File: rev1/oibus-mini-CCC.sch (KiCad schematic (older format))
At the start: 81 parts, among them J1 Conn_01x04_Female, J2 USB_B_Micro, J3 uavcan_5pins, J4 Conn_01x02_Female, P1 TC2030-MCP, Q1 DMG3415U-7, Q2 DMG3415U-7, Q3 DMG3415U-7, SW1 SW_Push, U1 AP2112K-3.3, U10 TPD3E001DRLR, U2 SAM-M8Q, U3 NINA-B311-00B, U4 MCP73831-2-OT, U5 MCP1624T, U6 SHT31-DIS-B, U7 TCAN330, U8 STM32F303CCTx, U9 DW01C-G, Y1 16M, Y2 32kHz

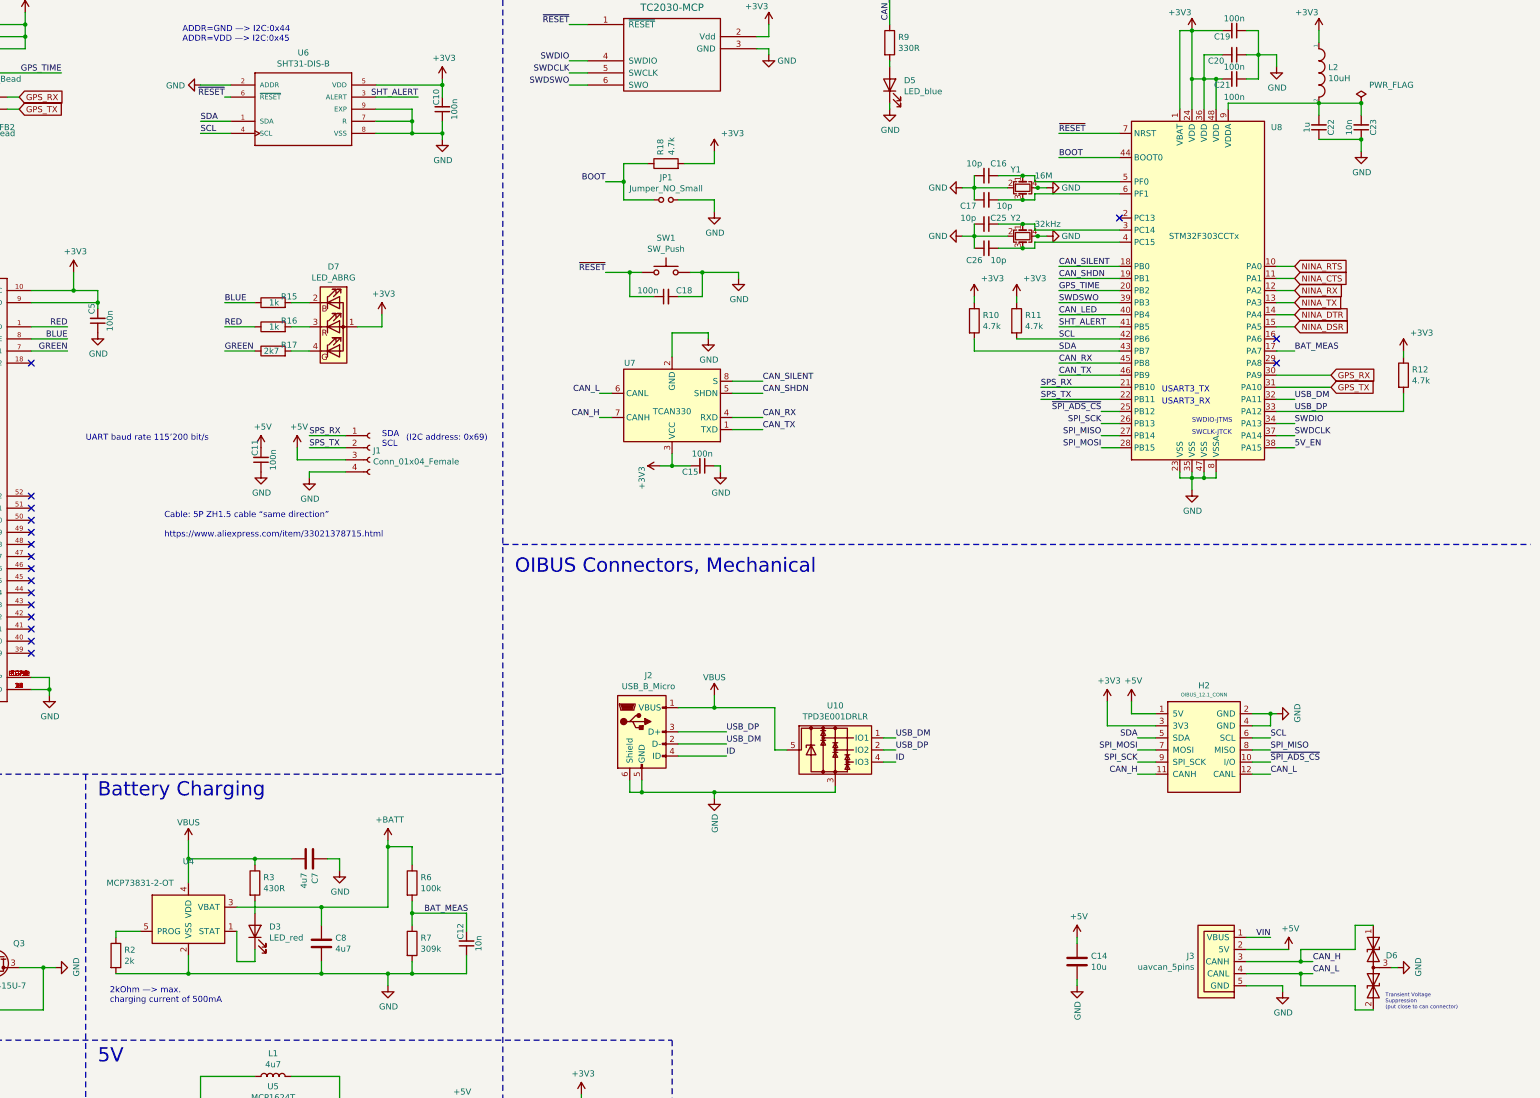
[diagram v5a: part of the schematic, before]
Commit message: finished routing, DRC clear
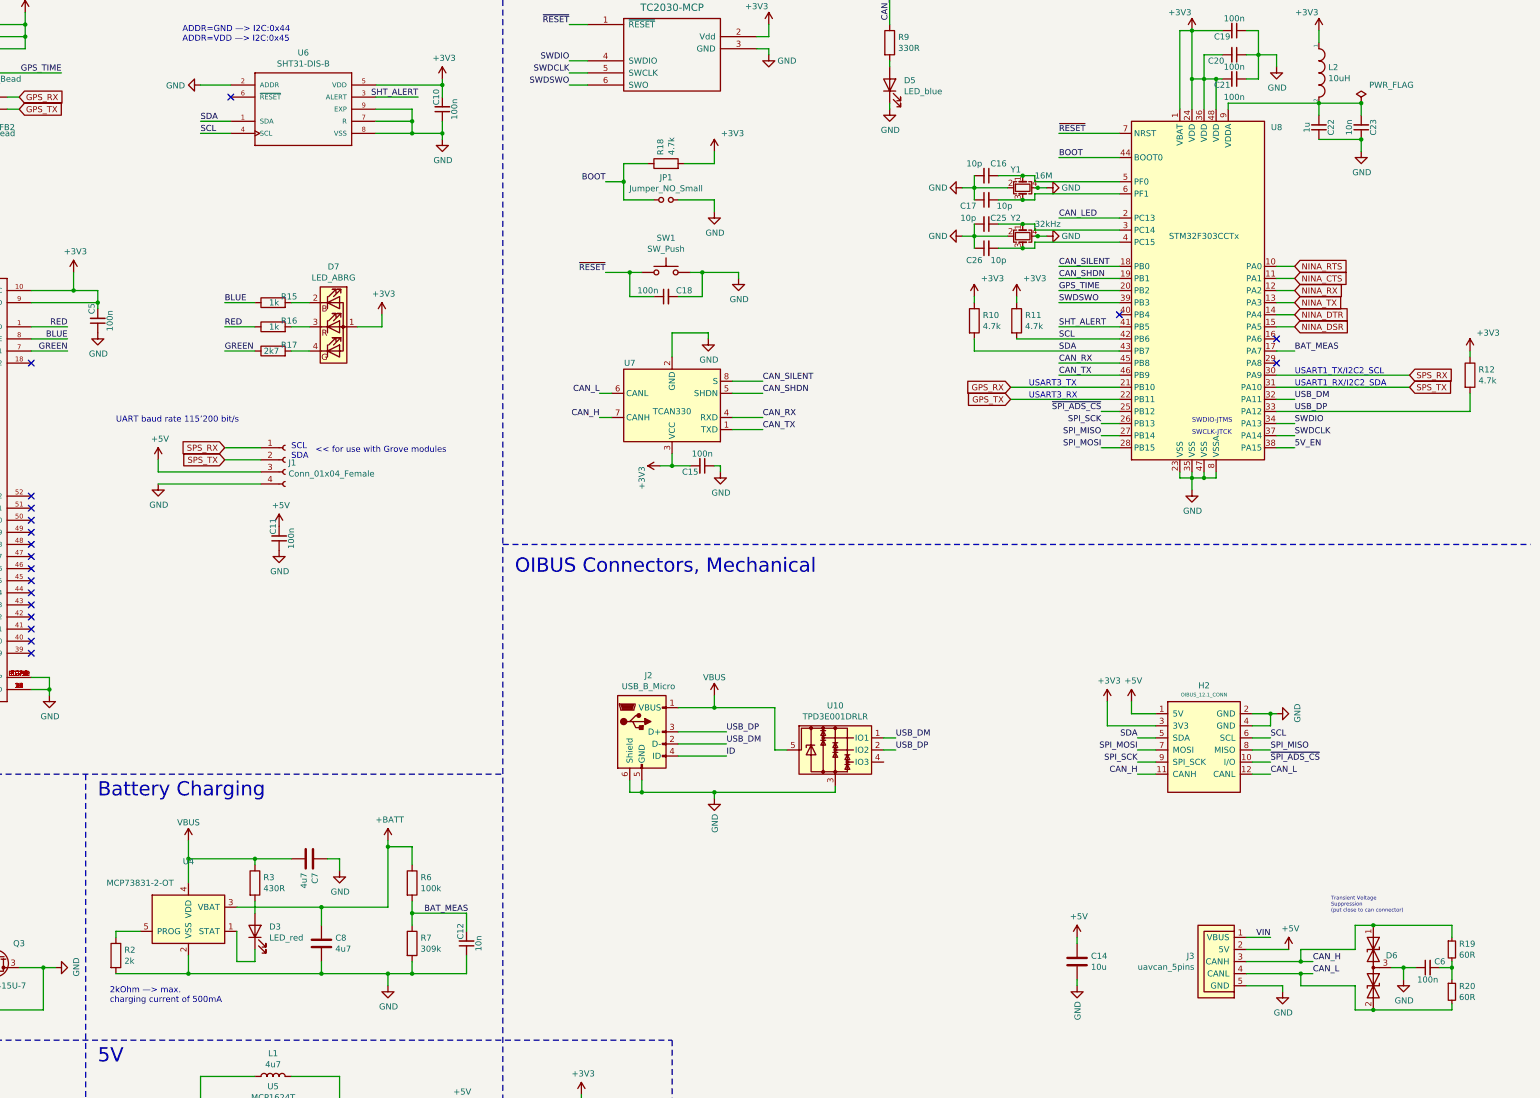
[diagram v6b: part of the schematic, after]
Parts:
- added C6: 100n, Capacitor_SMD:C_0603_1608Metric, symbol Device:C_Small
- added R19, R20: 60R, Resistor_SMD:R_0603_1608Metric, symbol Device:R_Small
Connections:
- net CAN_H: now also R19.1
- net CAN_L: now also R20.2
- net CAN_LED: now also U8.2 (PC13); no longer U8.40 (PB4)
- net GND: now also C6.1
- net GPS_RX: now also U8.21 (PB10); no longer U8.30 (PA9)
- net GPS_TX: now also U8.22 (PB11); no longer U8.31 (PA10)
- net ID: no longer U10.4 (IO3)
- net SPS_RX: now also U8.30 (PA9); no longer U8.21 (PB10)
- net SPS_TX: now also U8.31 (PA10); no longer U8.22 (PB11)
- net ~RESET: no longer U6.6 (~RESET~)
- new net: C6.2, R19.2, R20.1
- no-connect marks 38 -> 39
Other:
- note added: "<< for use with Grove modules"
- note added: "SCL\nSDA"
- note added: "USART1_RX/I2C2_SDA"
- note added: "USART1_TX/I2C2_SCL"
- note removed: "(I2C address: 0x69)"
- note removed: "Cable: 5P ZH1.5 cable “same direction”\n\nhttps://www.aliexpress.com/item/33021378715.html\n"
- note removed: "SDA\nSCL\n"
- moved on the sheet: C11, J1, R12

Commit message: performed some last fixes. Ready to review
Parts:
- removed JP1: Jumper_NO_Small, Jumper:SolderJumper-2_P1.3mm_Open_RoundedPad1.0x1.5mm, symbol Device:Jumper_NO_Small
- BT1: LCSC (none) -> C160352; MPN (none) -> B2B-PH-SM4-TB(LF)(SN)
- C16, C17, C25, C26: MPN 885012006051 -> (none)
- D1: footprint Diode_SMD:D_0603_1608Metric -> Diode_SMD:D_SOD-123F; MPN MBR120 -> MBR120ESFT1G
- FB1, FB2: MPN BLM15HD102SN1 -> BLM15HD102SN1D
- J1: Field4 (none) -> NOTE: MPN is for 10 pieces!; LCSC (none) -> 1125R-4p; MPN (none) -> 110990037
- J2: MPN (none) -> 1050170001
- J3: MPN (none) -> 0530480510
- Q2, Q3: value DMG3415U-7 -> NMOS; MPN DMG3415U-7 -> ZXMN3F30FHTA
- R1, R10, R11, R12, R18, R2, R4, R5, R6, R7: MPN RC0603FR-074K7L -> (none)
- R13, R14, R15, R16, R17, R3, R8, R9: MPN RC0603FR-07330RL -> (none)
- U1: MPN AP2112K-3.3 -> AP2112K-3.3TRG1
- U10: MPN (none) -> TPD3E001DRLR
- U2: MPN SAM-M8Q -> SAM-M8Q-0-10
- U4: MPN MCP73831-2-OT -> MCP73831T-2ATI/OT
- U5: MPN MCP1624T -> MCP1624T-I/CHY
- Y1: MPN FA-238 16.0000MA30X-AG0 -> XXBBBCNANF-16M
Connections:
- net BOOT: now also SW1.1
- net GND: now also Q3.2 (S); no longer Q3.3 (D)
- net ~RESET: no longer SW1.1
- net at Q2.3 (D): now also Q3.3 (D); no longer Q3.2 (S)
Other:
- moved on the sheet: C18, SW1

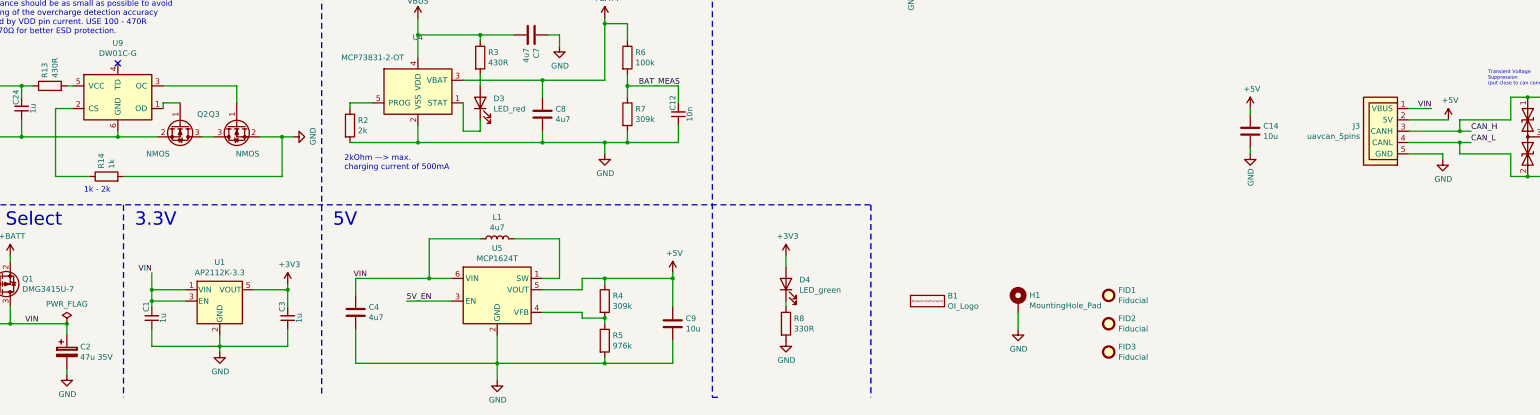
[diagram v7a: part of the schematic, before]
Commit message: moved the grove connector inside
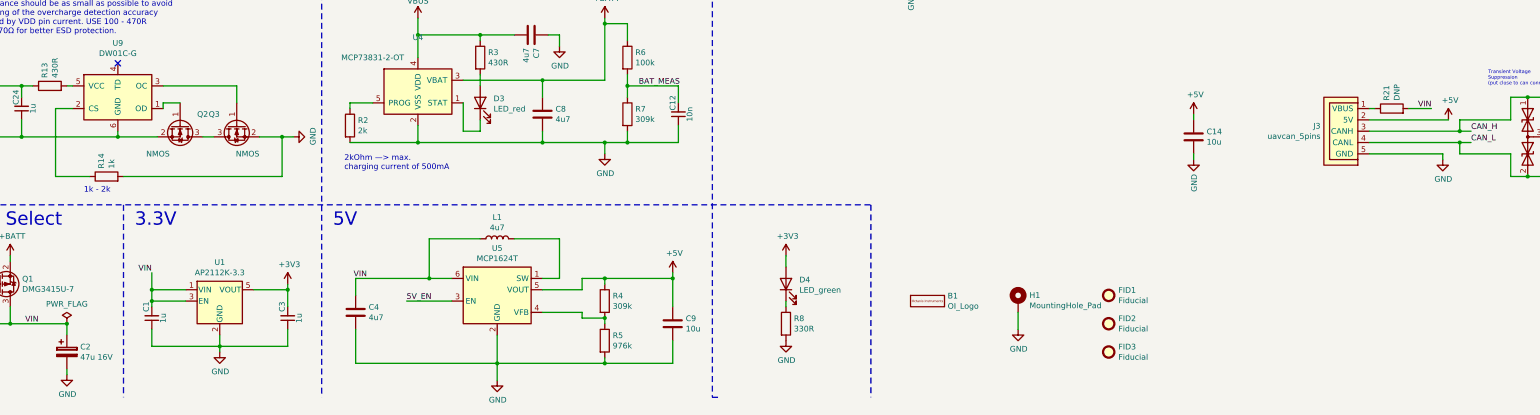
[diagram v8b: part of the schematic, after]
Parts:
- added R21: DNP, Resistor_SMD:R_0603_1608Metric, symbol Device:R
- C2: value 47u 35V -> 47u 16V; LCSC (none) -> C178535; MPN EMZR350ARA470ME61G -> EEEFK1C470UR
- D3: MPN IN-S63ASR -> (none)
- D4: MPN LTST-S270GKT -> (none)
- D5: MPN IN-S63AS5B -> (none)
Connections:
- net VIN: now also R21.2; no longer J3.1 (VBUS)
- new net: J3.1 (VBUS), R21.1
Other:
- moved on the sheet: C14, J3
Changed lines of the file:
@@
 F 2 "LED_SMD:LED_0603_1608Metric" H 5500 8600 50  0001 C CNN
 F 3 "~" H 5500 8600 50  0001 C CNN
-F 4 "IN-S63ASR" H -9550 5400 50  0001 C CNN "MPN"
+F 4 "" H -9550 5400 50  0001 C CNN "MPN"
 	1    5500 8600
 	0    -1   -1   0
@@
 P 1850 10800
 F 0 "C2" H 1968 10846 50  0000 L CNN
-F 1 "47u 35V" H 1968 10755 50  0000 L CNN
+F 1 "47u 16V" H 1968 10755 50  0000 L CNN
 F 2 "Capacitor_SMD:C_Elec_5x5.4" H 1888 10650 50  0001 C CNN
 F 3 "~" H 1850 10800 50  0001 C CNN
-F 4 "EMZR350ARA470ME61G" H -100 2000 50  0001 C CNN "MPN"
+F 4 "EEEFK1C470UR" H -100 2000 50  0001 C CNN "MPN"
+F 5 "C178535" H 0   0   50  0001 C CNN "LCSC"
 	1    1850 10800
 	1    0    0    -1
@@
 L Device:C C14
 U 1 1 5CCCB764
-P 12300 8850
-F 0 "C14" H 12185 8804 50  0000 R CNN
-F 1 "10u" H 12185 8895 50  0000 R CNN
-F 2 "Capacitor_SMD:C_0805_2012Metric" H 12338 8700 50  0001 C CNN
-F 3 "~" H 12300 8850 50  0001 C CNN
-F 4 "" H -50 550 50  0001 C CNN "MPN"
-	1    12300 8850
+P 11800 8900
+F 0 "C14" H 11685 8854 50  0000 R CNN
+F 1 "10u" H 11685 8945 50  0000 R CNN
+F 2 "Capacitor_SMD:C_0805_2012Metric" H 11838 8750 50  0001 C CNN
+F 3 "~" H 11800 8900 50  0001 C CNN
+F 4 "" H -550 600 50  0001 C CNN "MPN"
+	1    11800 8900
 	-1   0    0    1
 $EndComp
@@
 L power:GND #PWR034
 U 1 1 5CCCB76C
-P 12300 9050
-F 0 "#PWR034" H 12300 8800 50  0001 C CNN
-F 1 "GND" V 12305 8922 50  0000 R CNN
-F 2 "" H 12300 9050 50  0001 C CNN
-F 3 "" H 12300 9050 50  0001 C CNN
-	1    12300 9050
+P 11800 9100
+F 0 "#PWR034" H 11800 8850 50  0001 C CNN
+F 1 "GND" V 11805 8972 50  0000 R CNN
+F 2 "" H 11800 9100 50  0001 C CNN
+F 3 "" H 11800 9100 50  0001 C CNN
+	1    11800 9100
 	1    0    0    -1
 $EndComp
@@
 L power:+5V #PWR033
 U 1 1 5CCCB773
-P 12300 8650
-F 0 "#PWR033" H 12300 8500 50  0001 C CNN
-F 1 "+5V" H 12315 8823 50  0000 C CNN
-F 2 "" H 12300 8650 50  0001 C CNN
-F 3 "" H 12300 8650 50  0001 C CNN
-	1    12300 8650
+P 11800 8700
+F 0 "#PWR033" H 11800 8550 50  0001 C CNN
+F 1 "+5V" H 11815 8873 50  0000 C CNN
+F 2 "" H 11800 8700 50  0001 C CNN
+F 3 "" H 11800 8700 50  0001 C CNN
+	1    11800 8700
 	1    0    0    -1
 $EndComp
@@
 Transient Voltage \nSuppression\n(put close to can connector)
 Wire Wire Line
-	12300 8650 12300 8700
-Wire Wire Line
-	12300 9000 12300 9050
+	11800 8700 11800 8750
+Wire Wire Line
+	11800 9050 11800 9100
 $Comp
 L Mechanical:Fiducial FID2
@@
 F 2 "LED_SMD:LED_0603_1608Metric" H 8200 10200 50  0001 C CNN
 F 3 "~" H 8200 10200 50  0001 C CNN
-F 4 "LTST-S270GKT" H -600 1400 50  0001 C CNN "MPN"
+F 4 "" H -600 1400 50  0001 C CNN "MPN"
 	1    8200 10200
 	0    -1   -1   0
@@
 F 2 "LED_SMD:LED_0603_1608Metric" H 10750 1600 50  0001 C CNN
 F 3 "~" H 10750 1600 50  0001 C CNN
-F 4 "IN-S63AS5B" H -4050 -2300 50  0001 C CNN "MPN"
+F 4 "" H -4050 -2300 50  0001 C CNN "MPN"
 	1    10750 1600
 	0    -1   -1   0
@@
 L uavcan_connector:uavcan_5pins J3
 U 1 1 5E0C7EA8
-P 13450 8900
-F 0 "J3" H 13270 8804 50  0000 R CNN
-F 1 "uavcan_5pins" H 13270 8895 50  0000 R CNN
-F 2 "lib_fp_global:Molex_PicoBlade_53048-0510_1x05_P1.25mm_Horizontal" V 13300 8900 50  0001 C CNN
-F 3 "~" V 13300 8900 50  0001 C CNN
-F 4 "0530480510" H 0   0   50  0001 C CNN "MPN"
-	1    13450 8900
+P 13100 8900
+F 0 "J3" H 12920 8804 50  0000 R CNN
+F 1 "uavcan_5pins" H 12920 8895 50  0000 R CNN
+F 2 "lib_fp_global:Molex_PicoBlade_53048-0510_1x05_P1.25mm_Horizontal" V 12950 8900 50  0001 C CNN
+F 3 "~" V 12950 8900 50  0001 C CNN
+F 4 "0530480510" H -350 0   50  0001 C CNN "MPN"
+	1    13100 8900
 	1    0    0    1
 $EndComp
 Wire Wire Line
-	13700 8650 13900 8650
+	13350 8650 13400 8650
 Text Label 13900 8650 2    50   ~ 0
 VIN
 Wire Wire Line
-	14050 8750 13700 8750
-Wire Wire Line
-	13700 8850 14150 8850
-Wire Wire Line
-	13700 8950 14150 8950
+	14050 8750 13350 8750
+Wire Wire Line
+	13350 8850 14150 8850
+Wire Wire Line
+	13350 8950 14150 8950
 $Comp
 L power:GND #PWR043
@@
 $EndComp
 Wire Wire Line
-	13700 9050 14000 9050
+	13350 9050 14000 9050
 Wire Wire Line
 	14000 9050 14000 9100
@@
 Wire Wire Line
 	9000 3150 9300 3150
+$Comp
+L Device:R R21
+U 1 1 5DC3369C
+P 13550 8650
+F 0 "R21" H 13620 8696 50  0000 L CNN
+F 1 "DNP" H 13620 8605 50  0000 L CNN
+F 2 "Resistor_SMD:R_0603_1608Metric" V 13480 8650 50  0001 C CNN
+F 3 "~" H 13550 8650 50  0001 C CNN
+	1    13550 8650
+	0    -1   -1   0
+$EndComp
+Wire Wire Line
+	13700 8650 13900 8650
 $EndSCHEMATC
